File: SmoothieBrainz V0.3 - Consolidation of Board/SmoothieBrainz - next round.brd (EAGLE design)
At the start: 101 x 101 mm, 218 parts, among them IC1 LPC1769, IC5 LD117ADT33TR, Q1 BSL207SP, Q2 12MHz, SW1 SW_TACT_4P_B, SW3 SW_TACT_4P_B, T1 BC817, U3 USD-SOCKETUSD, X1 MSTBA2, X14 USBPTH, X2 GMSTBA2, X3 GMSTBA4, X4 1751248, X5 1751248, X6 1751248, X7 1751248

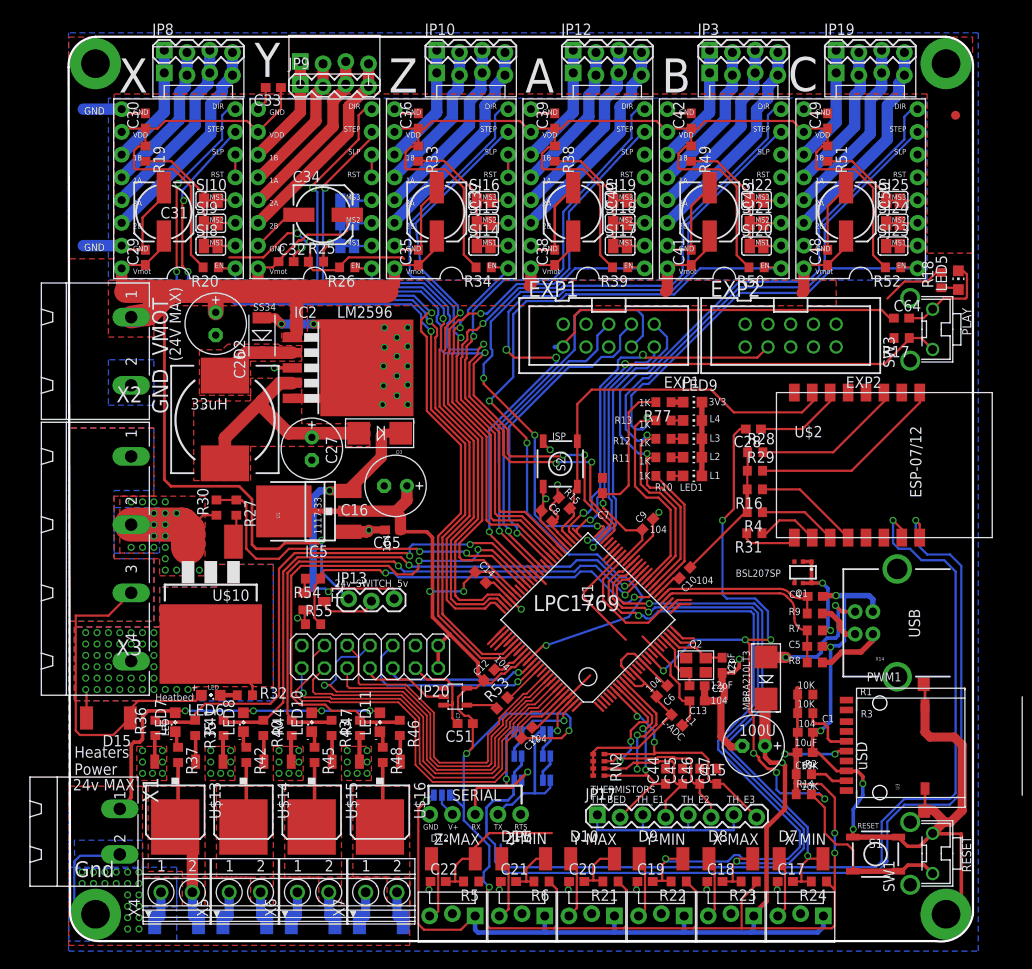
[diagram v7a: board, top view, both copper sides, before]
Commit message: major routing complete
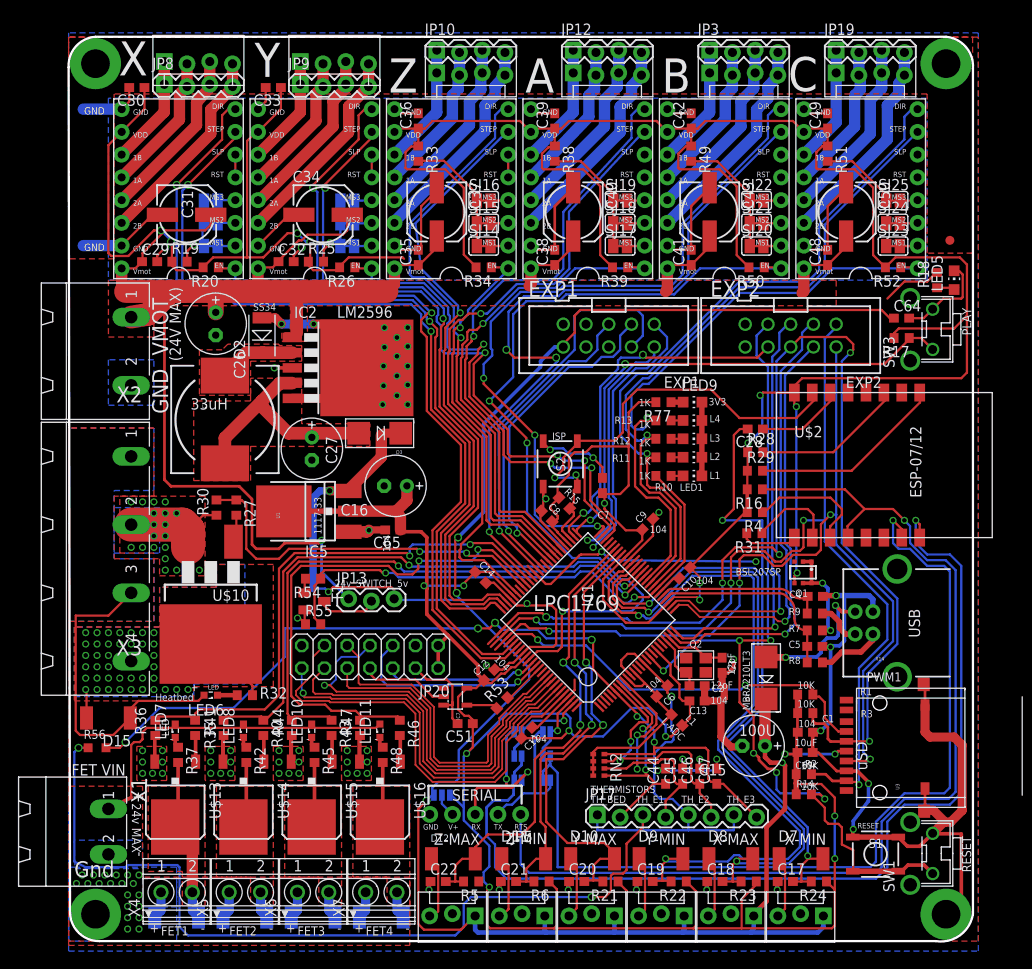
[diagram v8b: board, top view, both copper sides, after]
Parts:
- added R56: THERM, varistor:CT/CN0603
- LED10, LED11, LED6, LED7, LED8: device led:SML0805 -> led:SML0603
- moved U$12 14.0 mm to (98.4, 78.3)
- moved R19 12.7 mm to (12.4, 75.9), turned to 0 degrees
- moved C30 3.85 mm to (7.62, 95.3), turned to 180 degrees
- moved JP8 3.81 mm to (10.7, 95.6)
- moved C31 2.56 mm to (13.2, 81.1), turned to 0 degrees
- moved X1 1.27 mm to (-0.64, 12.2)
- moved JP6 1.27 mm to (10.7, 98.1)
- moved LED10 0.95 mm to (27.1, 23.5)
- moved LED11 0.95 mm to (34.8, 23.5)
- moved LED7 0.95 mm to (11.9, 23.5)
- moved LED8 0.95 mm to (19.5, 23.5)
- moved C29 0.67 mm to (9.05, 75.9), turned to 0 degrees
- moved D13 0.63 mm to (27.3, 2.70)
- moved D14 0.63 mm to (34.9, 2.70)
- moved D5 0.63 mm to (12.1, 2.70)
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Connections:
- net AGND: now also R56.1
- net TH4: now also R56.2
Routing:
- net 3.3V: track 523.2 -> 660.3 mm, vias 13 -> 21
- net AGND: track 31.2 -> 160.2 mm, vias 0 -> 7
- net SD_MOSI: track 8.44 -> 130.5 mm, vias 0 -> 5
- net SD_MISO: track 6.31 -> 111.7 mm, vias 0 -> 4
- net RTS: track 11.8 -> 116.5 mm, vias 0 -> 1
- net SD_SCK: track 1.96 -> 104.2 mm, vias 0 -> 4
- net 5V: track 175.6 -> 246.9 mm, vias 4 -> 6
- net TH4: track 30.5 -> 100.8 mm, vias 2 -> 6
- net SD_WP-ENC-B-ON-RRD: track 1.94 -> 48.7 mm, vias 0 -> 1
- net SD-CD-ON-RRD: track 2.47 -> 47.3 mm, vias 0 -> 1
- net SD-CS-ON-RRD: track 2.88 -> 47.7 mm, vias 0 -> 1
- net SD_CS: track 0.95 -> 45.0 mm, vias 0 -> 2
- net SD_IRQ-ENC-A-ON-RRD: track 2.42 -> 46.4 mm, vias 0 -> 1
- net Z_MIN: track 8.21 -> 47.1 mm, vias 0 -> 2
- net Z_MAX: track 18.7 -> 52.3 mm, vias 0 -> 2
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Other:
- board text added: "FET VIN"
- board text added: "FET1"
- board text added: "FET2"
- board text added: "FET3"
- board text added: "FET4"
- board text removed: "Heaters Power"
